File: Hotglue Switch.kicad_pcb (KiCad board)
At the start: 2 copper layers, 26 x 10.2 mm, 10 parts, among them J3 BATTERY, J8 +OUTPUT, J9 -OUTPUT, M1 Screw, M2 Screw

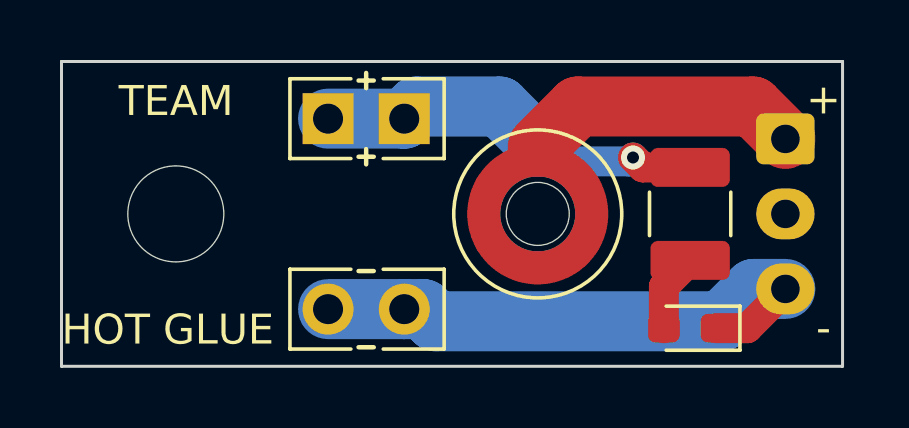
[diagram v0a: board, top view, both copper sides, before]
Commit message: Update Hotglue Switch.kicad_pcb
fixed pcb thickness to 0.8mm for standoff clearance.
Replaced routed tracks with polygon pours
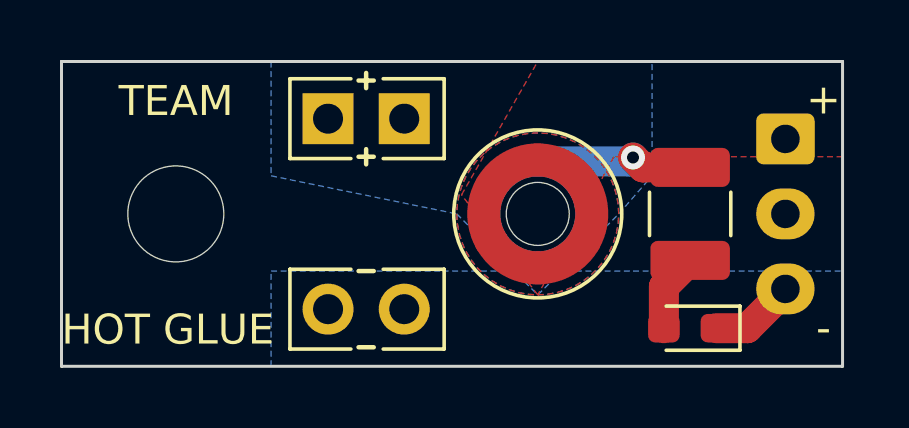
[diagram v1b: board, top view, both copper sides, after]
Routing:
- net -BATT: track 18.7 -> 2.87 mm
- net +BATT: track 9.25 -> 0.00 mm
- net /BATT SWITCH: track 13.0 -> 5.27 mm
- added copper zone on F.Cu, net +BATT
- added copper zone on B.Cu, net -BATT
- added copper zone on B.Cu, net /BATT SWITCH
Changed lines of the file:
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@@
 	(generator_version "8.0")
 	(general
-		(thickness 0.6)
+		(thickness 0.8)
 		(legacy_teardrops no)
 	)
@@
 			(layer "dielectric 1"
 				(type "core")
-				(thickness 0.51)
+				(thickness 0.71)
 				(material "FR4")
 				(epsilon_r 4.5)
@@
 	)
 	(segment
-		(start 76.195 47.625)
-		(end 76.6 47.22)
-		(width 2)
-		(layer "B.Cu")
-		(net 1)
-	)
-	(segment
 		(start 83.69 49.05)
 		(end 80.645 49.05)
 		(width 1)
-		(layer "B.Cu")
-		(net 1)
-	)
-	(segment
-		(start 76.6 47.22)
-		(end 79.375 47.22)
-		(width 2)
 		(layer "B.Cu")
 		(net 1)
@@
 	)
 	(segment
-		(start 73.655 47.625)
-		(end 76.195 47.625)
-		(width 2)
-		(layer "B.Cu")
-		(net 1)
-	)
-	(segment
-		(start 80.645 48.49)
-		(end 80.645 48.55)
-		(width 2)
-		(layer "B.Cu")
-		(net 1)
-	)
-	(segment
-		(start 79.375 47.22)
-		(end 80.645 48.49)
-		(width 2)
-		(layer "B.Cu")
-		(net 1)
-	)
-	(segment
 		(start 84.85 53.225)
 		(end 85.725 52.35)
@@
 		(net 3)
 	)
-	(segment
-		(start 87.845 53.3)
-		(end 88.9 53.3)
-		(width 2)
+	(zone
+		(net 4)
+		(net_name "+BATT")
+		(layer "F.Cu")
+		(name "top bat+")
+		(hatch edge 0.5)
+		(priority 4)
+		(connect_pads thru_hole_only
+			(clearance 0.5)
+		)
+		(min_thickness 0.1)
+		(filled_areas_thickness no)
+		(fill yes
+			(thermal_gap 0.25)
+			(thermal_bridge_width 1)
+			(smoothing fillet)
+			(radius 2)
+		)
+		(polygon
+			(pts
+				(xy 83.345 50.8) (xy 83.325314 50.474551) (xy 83.266543 50.153848) (xy 83.169544 49.842567) (xy 83.035731 49.545247)
+				(xy 82.867056 49.266225) (xy 82.665979 49.009569) (xy 82.435431 48.779021) (xy 82.178775 48.577944)
+				(xy 81.899753 48.409269) (xy 81.602433 48.275456) (xy 81.291152 48.178457) (xy 80.970449 48.119686)
+				(xy 80.645 48.1) (xy 80.319551 48.119686) (xy 79.998848 48.178457) (xy 79.687567 48.275456) (xy 79.390247 48.409269)
+				(xy 79.111225 48.577944) (xy 78.854569 48.779021) (xy 78.624021 49.009569) (xy 78.422944 49.266225)
+				(xy 78.254269 49.545247) (xy 78.120456 49.842567) (xy 78.023457 50.153848) (xy 77.964686 50.474551)
+				(xy 77.945 50.8) (xy 77.964686 51.125449) (xy 78.023457 51.446152) (xy 78.120456 51.757433) (xy 78.254269 52.054753)
+				(xy 78.422944 52.333775) (xy 78.624021 52.590431) (xy 78.854569 52.820979) (xy 79.111225 53.022056)
+				(xy 79.390247 53.190731) (xy 79.687567 53.324544) (xy 79.998848 53.421543) (xy 80.319551 53.480314)
+				(xy 80.645 53.5) (xy 80.970449 53.480314) (xy 81.291152 53.421543) (xy 81.602433 53.324544) (xy 81.899753 53.190731)
+				(xy 82.178775 53.022056) (xy 82.435431 52.820979) (xy 82.665979 52.590431) (xy 82.867056 52.333775)
+				(xy 83.035731 52.054753) (xy 83.169544 51.757433) (xy 83.266543 51.446152) (xy 83.325314 51.125449)
+				(xy 83.345 50.8)
+			)
+		)
+	)
+	(zone
+		(net 4)
+		(net_name "+BATT")
+		(layer "F.Cu")
+		(name "top bat+")
+		(hatch edge 0.5)
+		(connect_pads thru_hole_only
+			(clearance 0.5)
+		)
+		(min_thickness 0.1)
+		(filled_areas_thickness no)
+		(fill yes
+			(thermal_gap 0.25)
+			(thermal_bridge_width 1)
+			(smoothing fillet)
+			(radius 2)
+		)
+		(polygon
+			(pts
+				(xy 90.805 45.72) (xy 90.805 48.895) (xy 83.185 48.895) (xy 80.645 53.5) (xy 80.645 53.5) (xy 78.105 50.165)
+				(xy 80.645 45.72)
+			)
+		)
+	)
+	(zone
+		(net 1)
+		(net_name "/BATT SWITCH")
 		(layer "B.Cu")
+		(name "bot bat sw")
+		(hatch edge 0.5)
+		(connect_pads thru_hole_only
+			(clearance 0.5)
+		)
+		(min_thickness 0.1)
+		(filled_areas_thickness no)
+		(fill yes
+			(thermal_gap 0.25)
+			(thermal_bridge_width 1)
+			(smoothing fillet)
+			(radius 2)
+		)
+		(polygon
+			(pts
+				(xy 71.755 45.72) (xy 71.755 49.53) (xy 77.945 50.8) (xy 80.645 53.5) (xy 80.645 53.5) (xy 83.345 50.8)
+				(xy 84.455 49.53) (xy 84.455 45.72)
+			)
+		)
+	)
+	(zone
 		(net 3)
-	)
-	(segment
-		(start 76.195 53.975)
-		(end 76.835 53.975)
-		(width 2)
+		(net_name "-BATT")
 		(layer "B.Cu")
-		(net 3)
-	)
-	(segment
-		(start 76.195 53.975)
-		(end 73.655 53.975)
-		(width 2)
+		(name "bot bat-")
+		(hatch edge 0.5)
+		(priority 1)
+		(connect_pads thru_hole_only
+			(clearance 0.5)
+		)
+		(min_thickness 0.1)
+		(filled_areas_thickness no)
+		(fill yes
+			(thermal_gap 0.25)
+			(thermal_bridge_width 1)
+			(smoothing fillet)
+			(radius 2)
+		)
+		(polygon
+			(pts
+				(xy 71.755 52.705) (xy 77.47 52.705) (xy 79.375 52.705) (xy 81.915 52.705) (xy 83.82 52.705) (xy 90.805 52.705)
+				(xy 90.805 55.88) (xy 71.755 55.88)
+			)
+		)
+	)
+	(zone
+		(net 1)
+		(net_name "/BATT SWITCH")
 		(layer "B.Cu")
-		(net 3)
-	)
-	(segment
-		(start 76.835 53.975)
-		(end 77.24 54.38)
-		(width 2)
-		(layer "B.Cu")
-		(net 3)
-	)
-	(segment
-		(start 86.765 54.38)
-		(end 87.845 53.3)
-		(width 2)
-		(layer "B.Cu")
-		(net 3)
-	)
-	(segment
-		(start 77.24 54.38)
-		(end 86.765 54.38)
-		(width 2)
-		(layer "B.Cu")
-		(net 3)
-	)
-	(segment
-		(start 88.9 48.3)
-		(end 87.82 47.22)
-		(width 2)
-		(layer "F.Cu")
-		(net 4)
-	)
-	(segment
-		(start 87.82 47.22)
-		(end 81.975 47.22)
-		(width 2)
-		(layer "F.Cu")
-		(net 4)
-	)
-	(segment
-		(start 81.975 47.22)
-		(end 80.645 48.55)
-		(width 2)
-		(layer "F.Cu")
-		(net 4)
+		(name "bot bat sw")
+		(hatch edge 0.5)
+		(priority 4)
+		(connect_pads thru_hole_only
+			(clearance 0.5)
+		)
+		(min_thickness 0.1)
+		(filled_areas_thickness no)
+		(fill yes
+			(thermal_gap 0.25)
+			(thermal_bridge_width 1)
+			(smoothing fillet)
+			(radius 2)
+		)
+		(polygon
+			(pts
+				(xy 83.345 50.8) (xy 83.325314 50.474551) (xy 83.266543 50.153848) (xy 83.169544 49.842567) (xy 83.035731 49.545247)
+				(xy 82.867056 49.266225) (xy 82.665979 49.009569) (xy 82.435431 48.779021) (xy 82.178775 48.577944)
+				(xy 81.899753 48.409269) (xy 81.602433 48.275456) (xy 81.291152 48.178457) (xy 80.970449 48.119686)
+				(xy 80.645 48.1) (xy 80.319551 48.119686) (xy 79.998848 48.178457) (xy 79.687567 48.275456) (xy 79.390247 48.409269)
+				(xy 79.111225 48.577944) (xy 78.854569 48.779021) (xy 78.624021 49.009569) (xy 78.422944 49.266225)
+				(xy 78.254269 49.545247) (xy 78.120456 49.842567) (xy 78.023457 50.153848) (xy 77.964686 50.474551)
+				(xy 77.945 50.8) (xy 77.964686 51.125449) (xy 78.023457 51.446152) (xy 78.120456 51.757433) (xy 78.254269 52.054753)
+				(xy 78.422944 52.333775) (xy 78.624021 52.590431) (xy 78.854569 52.820979) (xy 79.111225 53.022056)
+				(xy 79.390247 53.190731) (xy 79.687567 53.324544) (xy 79.998848 53.421543) (xy 80.319551 53.480314)
+				(xy 80.645 53.5) (xy 80.970449 53.480314) (xy 81.291152 53.421543) (xy 81.602433 53.324544) (xy 81.899753 53.190731)
+				(xy 82.178775 53.022056) (xy 82.435431 52.820979) (xy 82.665979 52.590431) (xy 82.867056 52.333775)
+				(xy 83.035731 52.054753) (xy 83.169544 51.757433) (xy 83.266543 51.446152) (xy 83.325314 51.125449)
+				(xy 83.345 50.8)
+			)
+		)
 	)
 )
